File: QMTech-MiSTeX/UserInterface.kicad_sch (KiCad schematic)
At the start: 58 parts, among them CN2 U.FL-R-SMT-1(80), CN3 U.FL-R-SMT-1(80), CN4 U.FL-R-SMT-1(80), CN5 U.FL-R-SMT-1(80), CN6 U.FL-R-SMT-1(80), CN7 U.FL-R-SMT-1(80), SW1 TS-1187A-B-A-B, SW2 TS-1187A-B-A-B, SW3 TS-1187A-B-A-B, SW4 TS-1187A-B-A-B, SW5 XKB5858-W-F-75

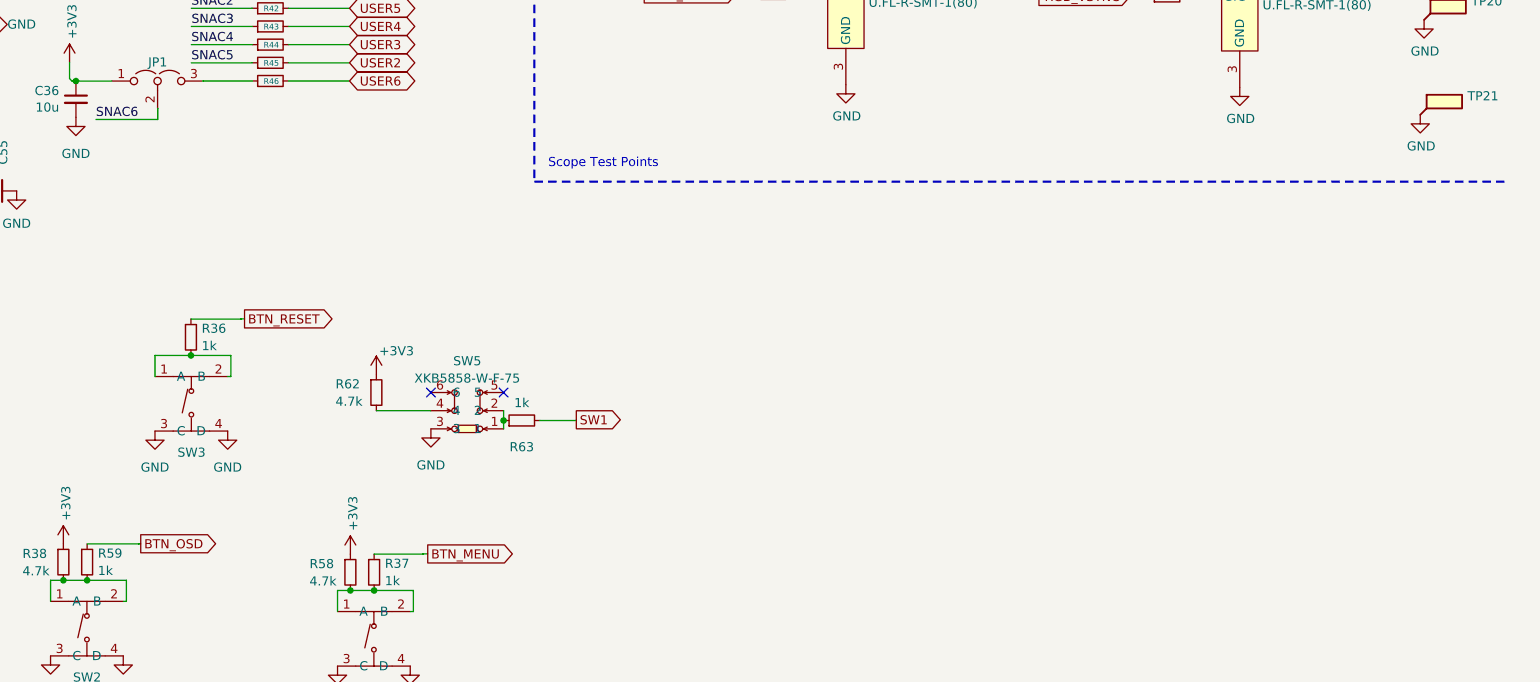
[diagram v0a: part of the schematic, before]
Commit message: connect two remaining pins to new 2 row Pmod, fix via, tidy test points
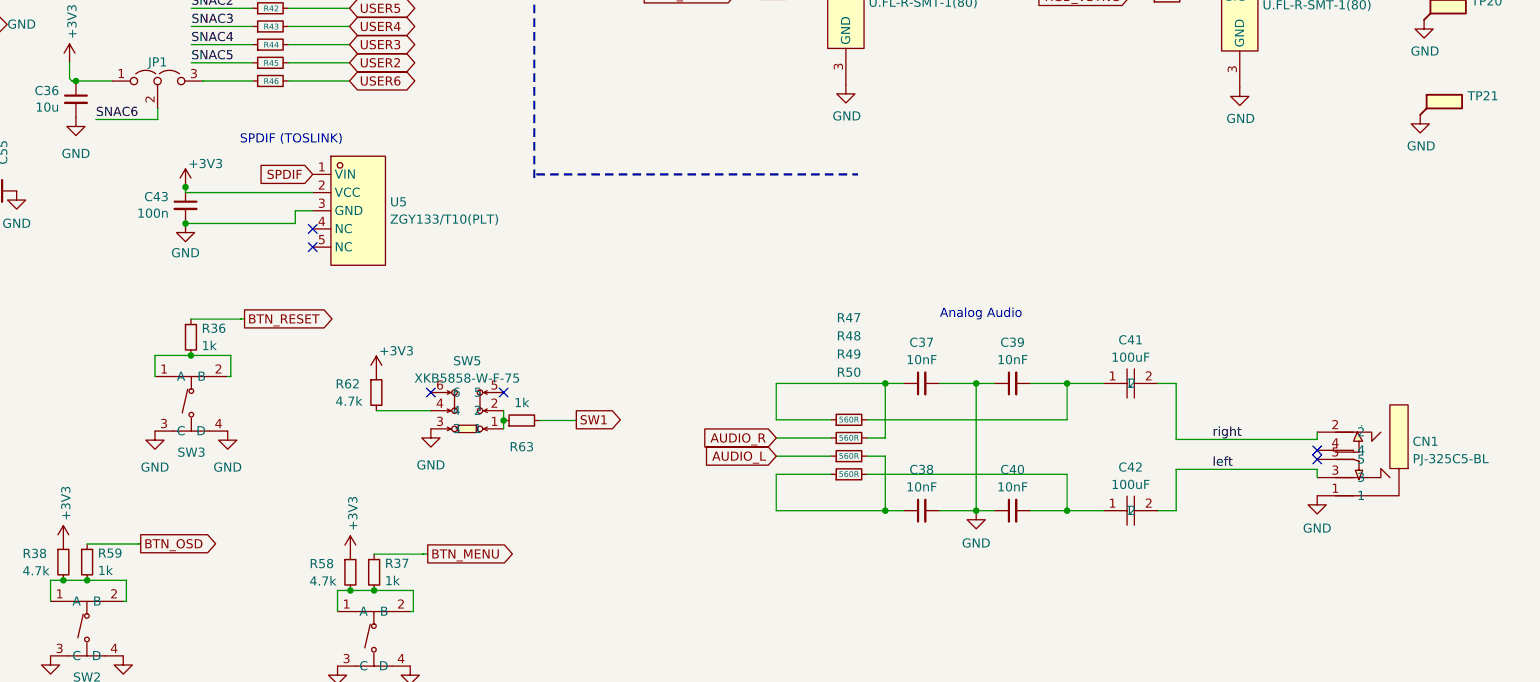
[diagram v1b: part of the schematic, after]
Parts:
- added C37, C38, C39, C40: 10nF, C_0402_1005Metric, symbol jlcpcb-basic-mlcc-0402:10nF
- added C41, C42: 100uF, easyeda2kicad:C1206, symbol easyeda2kicad:CL31A107MQHNNNE
- added C43: 100n, Capacitor_SMD:C_0603_1608Metric, symbol Device:C_Small
- added CN1: PJ-325C5-BL, easyeda2kicad:TH_PJ-325C5-B, symbol easyeda2kicad:PJ-325C5-BL
- added R47, R48, R49, R50: 560R, R_0603_1608Metric, symbol jlcpcb-basic-resistor-0603:560R
- added U5: ZGY133/T10(PLT), easyeda2kicad:COMM-TH_ZGY133-T10-PLT, symbol easyeda2kicad:ZGY133_T10(PLT)
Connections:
- net +3V3: now also C43.1, U5.2 (VCC)
- net GND: now also C37.2, C38.2, C39.1, C40.1, C43.2, CN1.1, U5.3 (GND)
- net SPDIF: now also U5.1 (VIN)
- new net: C37.1, R47.1, R48.2
- new net: C39.2, C41.1, R47.2
- new net: C38.1, R49.2, R50.1
- new net: C40.2, C42.1, R50.2
- new net AUDIO_L: R49.1
- new net AUDIO_R: R48.1
- new net left: C42.2, CN1.3
- new net right: C41.2, CN1.2
- no-connect marks 4 -> 8
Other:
- note added: "Analog Audio"
- note added: "SPDIF (TOSLINK)"
- note removed: "Scope Test Points"

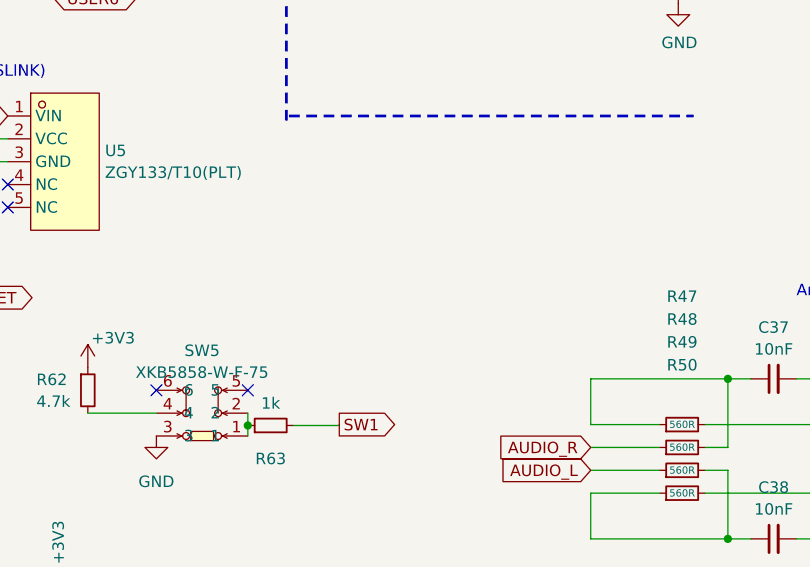
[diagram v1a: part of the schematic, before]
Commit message: add front switch, reroute USB, test points
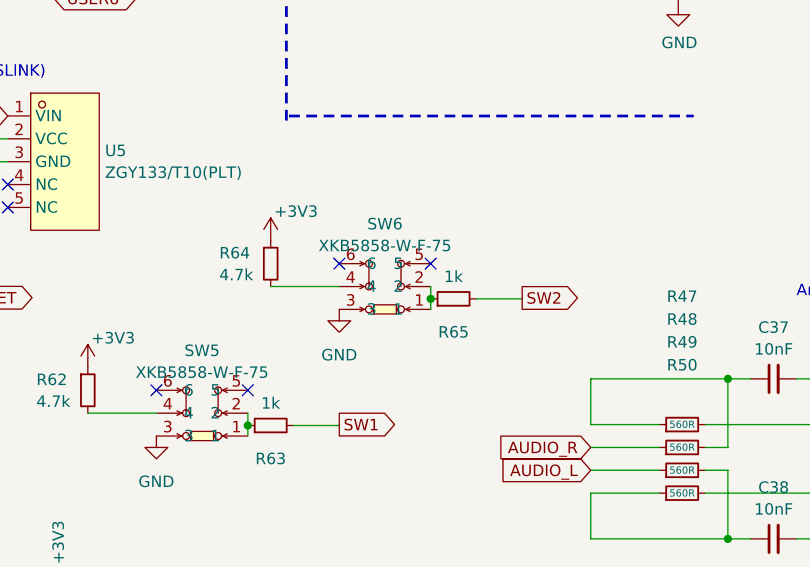
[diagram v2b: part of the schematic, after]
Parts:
- added R64: 4.7k, R_0402_1005Metric, symbol jlcpcb-basic-resistor:R_0402_4.7k
- added R65: 1k, R_0402_1005Metric, symbol jlcpcb-basic-resistor-0402:1k
- added SW6: XKB5858-W-F-75, easyeda2kicad:SW-SMD_XKB5858-W-F-75, symbol easyeda2kicad:XKB5858-W-F-75
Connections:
- net +3V3: now also R64.1
- net GND: now also SW6.3
- new net: R65.1, SW6.1, SW6.2
- new net: R64.2, SW6.4
- new net SW2: R65.2
- no-connect marks 8 -> 10
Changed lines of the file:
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@@
   (junction (at 92.71 121.158) (diameter 0) (color 0 0 0 0)
   )
+  (junction (at 157.48 134.62) (diameter 0) (color 0 0 0 0)
+  )
   (junction (at 55.7022 66.7512) (diameter 0) (color 0 0 0 0)
   )
@@
   (no_connect (at 250.8504 152.8572))
   (no_connect (at 110.49 124.46))
+  (no_connect (at 147.32 130.7099))
+  (no_connect (at 157.48 130.7099))
   (no_connect (at 35.0774 88.2396))
   (no_connect (at 127 144.78))
@@
     (stroke (width 0) (type default))
   )
+  (wire (pts (xy 162.56 134.62) (xy 167.64 134.62))
+    (stroke (width 0) (type default))
+  )
   (wire (pts (xy 137.16 147.32) (xy 137.16 148.6901))
     (stroke (width 0) (type default))
@@
     (stroke (width 0) (type default))
   )
+  (wire (pts (xy 157.48 133.2499) (xy 157.48 134.62))
+    (stroke (width 0) (type default))
+  )
   (wire (pts (xy 198.12 143.51) (xy 203.2 143.51))
     (stroke (width 0) (type default))
@@
     (stroke (width 0) (type default))
   )
+  (wire (pts (xy 157.48 134.62) (xy 157.48 135.7899))
+    (stroke (width 0) (type default))
+  )
   (wire (pts (xy 93.5171 96.1644) (xy 102.0318 96.1644))
     (stroke (width 0) (type default))
@@
     (stroke (width 0) (type default))
   )
+  (wire (pts (xy 139.7 133.2499) (xy 147.32 133.2499))
+    (stroke (width 0) (type default))
+  )
   (wire (pts (xy 84.9687 52.7558) (xy 76.454 52.7558))
     (stroke (width 0) (type default))
@@
     (stroke (width 0.254) (type default))
   )
+  (wire (pts (xy 167.64 134.62) (xy 167.64 134.5199))
+    (stroke (width 0) (type default))
+  )
   (wire (pts (xy 228.6 143.51) (xy 231.14 143.51))
     (stroke (width 0.254) (type default))
@@
     )
   )
+  (global_label "SW2" (shape output) (at 167.64 134.5199 0) (fields_autoplaced)
+    (effects (font (size 1.27 1.27)) (justify left))
+    (property "Intersheetrefs" "${INTERSHEET_REFS}" (at 174.5907 134.5199 0)
+      (effects (font (size 1.27 1.27)) (justify left))
+    )
+  )
   (global_label "BTN_MENU" (shape output) (at 126.5557 167.3352 0) (fields_autoplaced)
     (effects (font (size 1.27 1.27)) (justify left))
@@
     )
   )
+  (symbol (lib_id "power:+3V3") (at 139.7 128.1699 0) (unit 1)
+    (in_bom yes) (on_board yes) (dnp no)
+    (property "Reference" "#PWR0186" (at 139.7 131.9799 0)
+      (effects (font (size 1.27 1.27)) hide)
+    )
+    (property "Value" "+3V3" (at 140.081 124.9187 0)
+      (effects (font (size 1.27 1.27)) (justify left))
+    )
+    (property "Footprint" "" (at 139.7 128.1699 0)
+      (effects (font (size 1.27 1.27)) hide)
+    )
+    (property "Datasheet" "" (at 139.7 128.1699 0)
+      (effects (font (size 1.27 1.27)) hide)
+    )
+    (pin "1")
+    (instances
+      (project "QMTech-MiSTeX"
+        (path "/bf95850e-2fcb-4784-a603-f17fc357556b/cce2b405-ae09-44af-ba42-d113d6ffe521"
+          (reference "#PWR0186") (unit 1)
+        )
+      )
+    )
+  )
   (symbol (lib_id "jlcpcb-basic-resistor-0402:1k") (at 227.5078 36.5506 90) (unit 1)
     (in_bom yes) (on_board yes) (dnp no) (fields_autoplaced)
@@
     )
   )
+  (symbol (lib_id "easyeda2kicad:XKB5858-W-F-75") (at 152.4 133.2499 90) (unit 1)
+    (in_bom yes) (on_board yes) (dnp no) (fields_autoplaced)
+    (property "Reference" "SW6" (at 152.4 126.3126 90)
+      (effects (font (size 1.27 1.27)))
+    )
+    (property "Value" "XKB5858-W-F-75" (at 152.4 128.7368 90)
+      (effects (font (size 1.27 1.27)))
+    )
+    (property "Footprint" "easyeda2kicad:SW-SMD_XKB5858-W-F-75" (at 165.1 133.2499 0)
+      (effects (font (size 1.27 1.27)) hide)
+    )
+    (property "Datasheet" "https://lcsc.com/product-detail/Electrical-Switches_XKB-Connectivity-XKB5858-W-F-75_C780037.html" (at 167.64 133.2499 0)
+      (effects (font (size 1.27 1.27)) hide)
+    )
+    (property "LCSC Part" "C780037" (at 170.18 133.2499 0)
+      (effects (font (size 1.27 1.27)) hide)
+    )
+    (pin "2")
+    (pin "1")
+    (pin "4")
+    (pin "5")
+    (pin "3")
+    (pin "6")
+    (instances
+      (project "QMTech-MiSTeX"
+        (path "/bf95850e-2fcb-4784-a603-f17fc357556b/cce2b405-ae09-44af-ba42-d113d6ffe521"
+          (reference "SW6") (unit 1)
+        )
+      )
+    )
+  )
   (symbol (lib_id "easyeda2kicad:TS-1187A-B-A-B") (at 119.0324 177.927 0) (unit 1)
     (in_bom yes) (on_board yes) (dnp no)
@@
     )
   )
+  (symbol (lib_id "jlcpcb-basic-resistor:R_0402_4.7k") (at 139.7 130.7099 0) (unit 1)
+    (in_bom yes) (on_board yes) (dnp no)
+    (property "Reference" "R64" (at 133.985 129.5415 0)
+      (effects (font (size 1.27 1.27)) (justify left))
+    )
+    (property "Value" "4.7k" (at 133.985 131.9657 0)
+      (effects (font (size 1.27 1.27)) (justify left))
+    )
+    (property "Footprint" "R_0402_1005Metric" (at 137.922 130.7099 90)
+      (effects (font (size 1.27 1.27)) hide)
+    )
+    (property "Datasheet" "https://datasheet.lcsc.com/szlcsc/Uniroyal-Elec-0402WGF4701TCE_C25900.pdf" (at 139.7 130.7099 90)
+      (effects (font (size 1.27 1.27)) hide)
+    )
+    (property "LCSC" "C25900" (at 139.7 130.7099 90)
+      (effects (font (size 1.27 1.27)) hide)
+    )
+    (pin "2")
+    (pin "1")
+    (instances
+      (project "QMTech-MiSTeX"
+        (path "/bf95850e-2fcb-4784-a603-f17fc357556b/cce2b405-ae09-44af-ba42-d113d6ffe521"
+          (reference "R64") (unit 1)
+        )
+      )
+    )
+  )
   (symbol (lib_id "jlcpcb-basic-resistor-0603:560R") (at 52.959 126.6698 180) (unit 1)
     (in_bom yes) (on_board yes) (dnp no) (fields_autoplaced)
@@
     )
   )
+  (symbol (lib_id "jlcpcb-basic-resistor-0402:1k") (at 160.02 134.62 90) (unit 1)
+    (in_bom yes) (on_board yes) (dnp no)
+    (property "Reference" "R65" (at 160.02 138.3299 90)
+      (effects (font (size 1.27 1.27)))
+    )
+    (property "Value" "1k" (at 160.02 132.1633 90)
+      (effects (font (size 1.27 1.27)))
+    )
+    (property "Footprint" "R_0402_1005Metric" (at 160.02 136.398 90)
+      (effects (font (size 1.27 1.27)) hide)
+    )
+    (property "Datasheet" "https://datasheet.lcsc.com/szlcsc/Uniroyal-Elec-0402WGF1001TCE_C11702.pdf" (at 160.02 134.62 90)
+      (effects (font (size 1.27 1.27)) hide)
+    )
+    (property "LCSC" "C11702" (at 160.02 134.62 90)
+      (effects (font (size 1.27 1.27)) hide)
+    )
+    (pin "2")
+    (pin "1")
+    (instances
+      (project "QMTech-MiSTeX"
+        (path "/bf95850e-2fcb-4784-a603-f17fc357556b/cce2b405-ae09-44af-ba42-d113d6ffe521"
+          (reference "R65") (unit 1)
+        )
+      )
+    )
+  )
   (symbol (lib_id "Device:C_Small") (at 92.71 118.618 0) (mirror y) (unit 1)
     (in_bom yes) (on_board yes) (dnp no)
@@
         )
       )
+    )
+  )
+  (symbol (lib_id "power:GND") (at 147.32 135.7899 0) (unit 1)
+    (in_bom yes) (on_board yes) (dnp no) (fields_autoplaced)
+    (property "Reference" "#PWR0187" (at 147.32 142.1399 0)
+      (effects (font (size 1.27 1.27)) hide)
+    )
+    (property "Value" "GND" (at 147.32 140.8699 0)
+      (effects (font (size 1.27 1.27)))
+    )
+    (property "Footprint" "" (at 147.32 135.7899 0)
+      (effects (font (size 1.27 1.27)) hide)
+    )
+    (property "Datasheet" "" (at 147.32 135.7899 0)
+      (effects (font (size 1.27 1.27)) hide)
+    )
+    (pin "1")
+    (instances
+      (project "QMTech-MiSTeX"
+        (path "/bf95850e-2fcb-4784-a603-f17fc357556b/cce2b405-ae09-44af-ba42-d113d6ffe521"
+          (reference "#PWR0187") (unit 1)
+        )
+      )

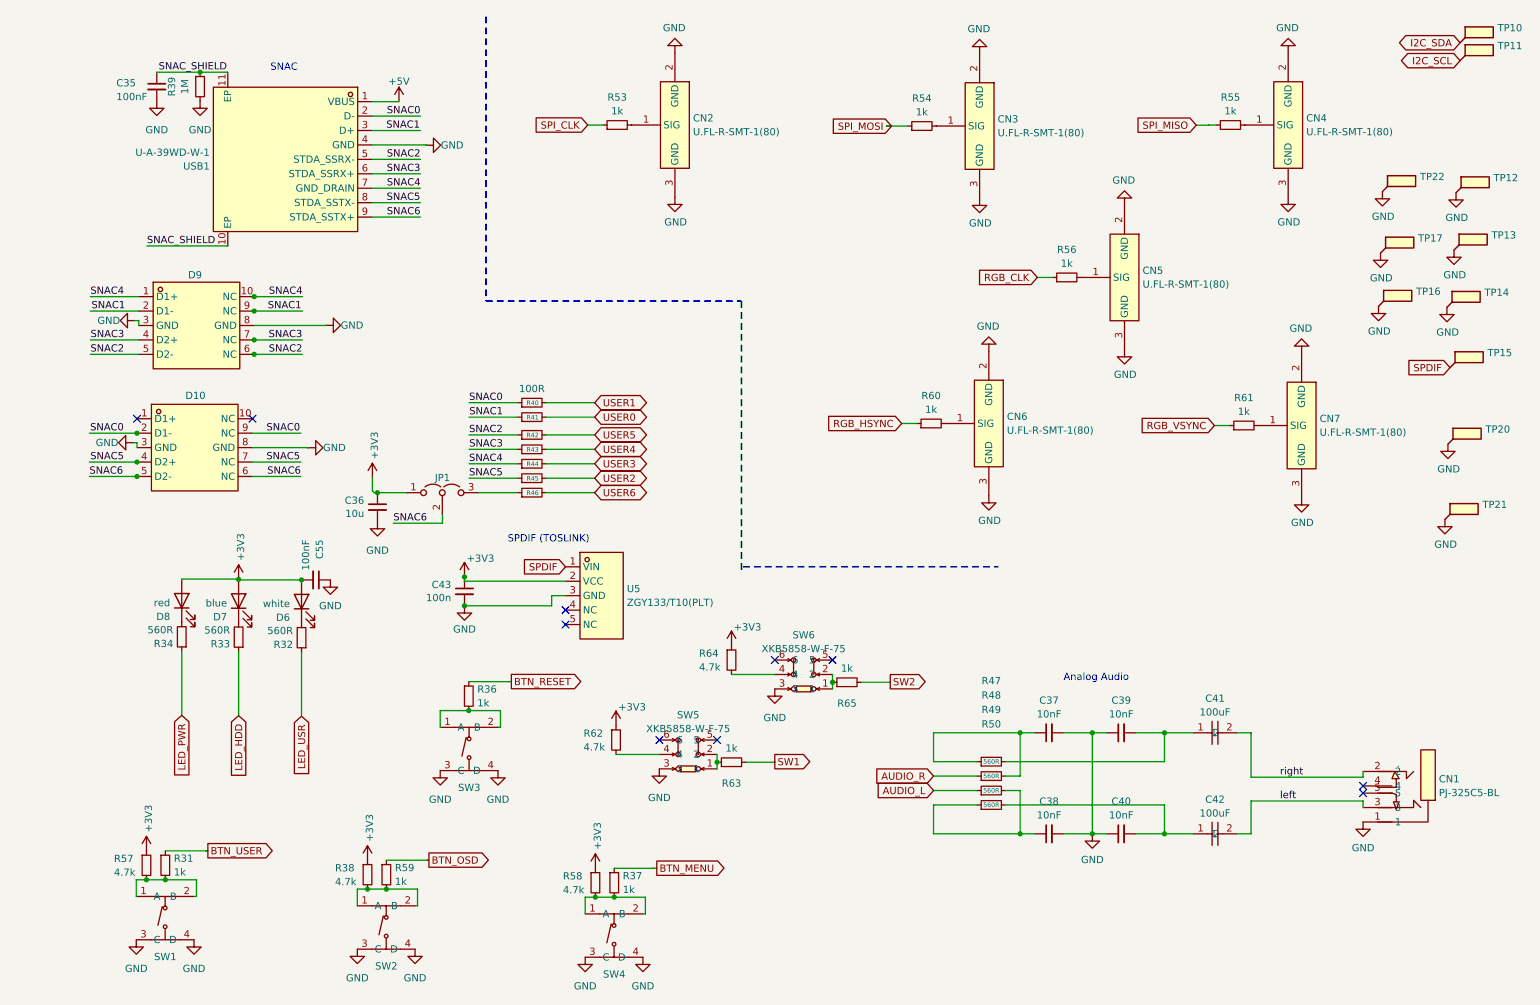
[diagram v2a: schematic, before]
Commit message: Add VGA green probe, add DIP switches, add to silk screen, cosmetics
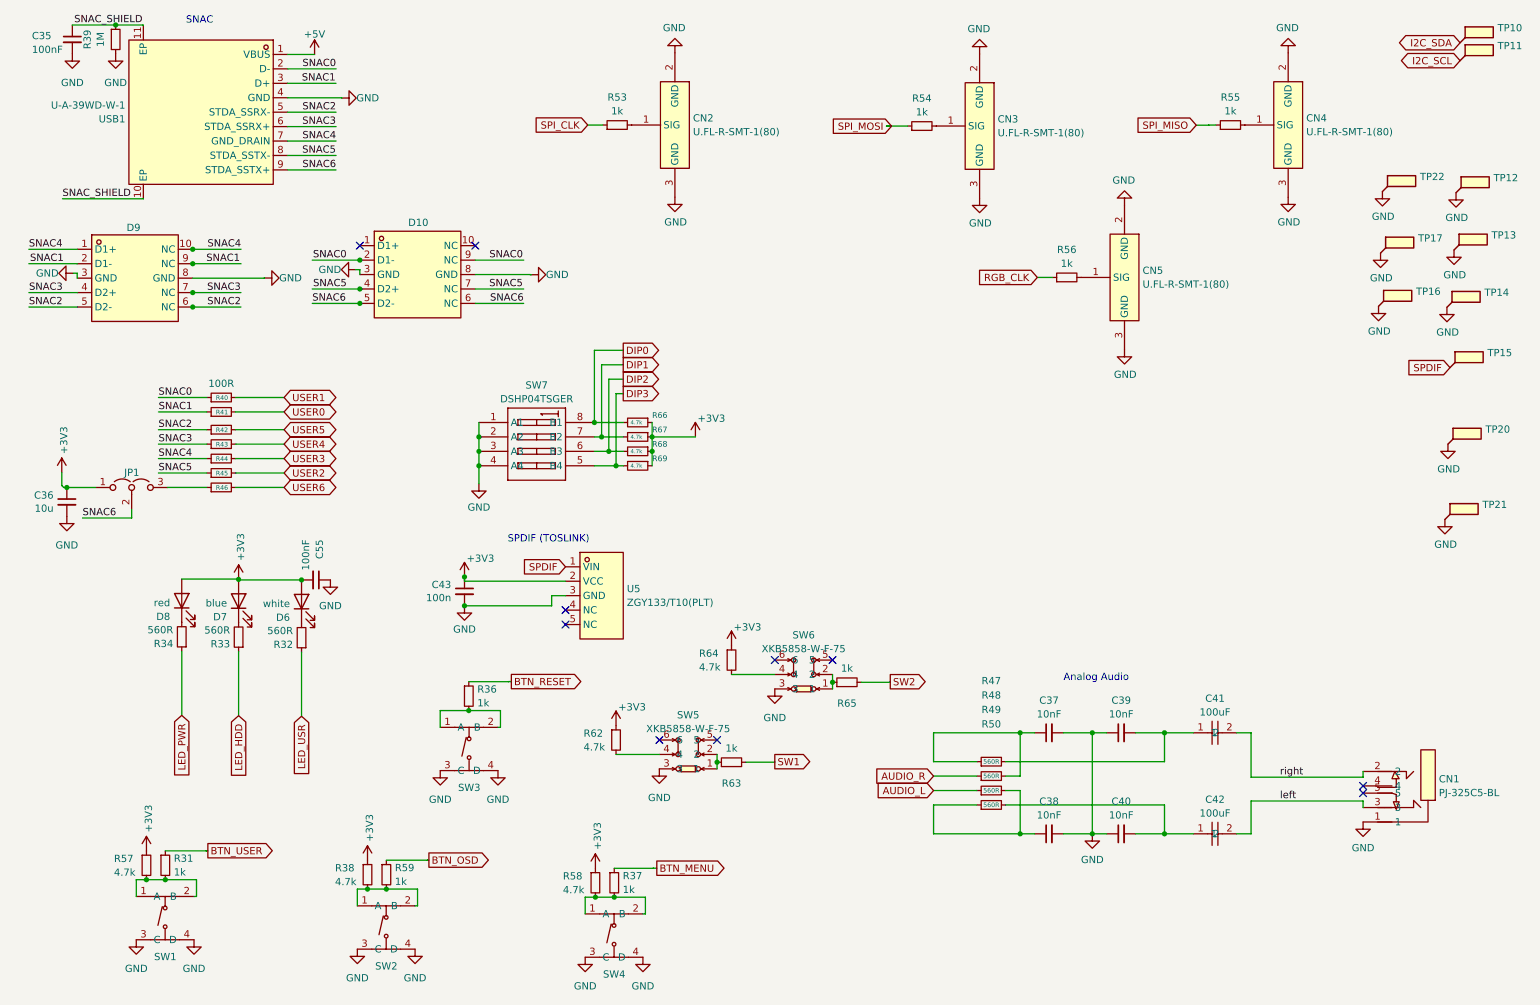
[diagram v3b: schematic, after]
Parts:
- removed CN6, CN7: U.FL-R-SMT-1(80), easyeda2kicad:RF-SMD_FRF05002-JSS103M, symbol easyeda2kicad:U.FL-R-SMT-1(80)
- removed R60, R61: 1k, R_0402_1005Metric, symbol jlcpcb-basic-resistor-0402:1k
- added R66, R67, R68, R69: 4.7k, R_0402_1005Metric, symbol jlcpcb-basic-resistor:R_0402_4.7k
- added SW7: DSHP04TSGER, easyeda2kicad:SW-SMD_8P-L6.7-W5.4-P1.27-LS8.4, symbol easyeda2kicad:DSHP04TSGER
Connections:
- net +3V3: now also R66.1, R67.1, R68.1, R69.1
- net GND: now also SW7.1 (A1), SW7.2 (A2), SW7.3 (A3), SW7.4 (A4)
- new net DIP0: R66.2, SW7.8 (B1)
- new net DIP1: R67.2, SW7.7 (B2)
- new net DIP2: R68.2, SW7.6 (B3)
- new net DIP3: R69.2, SW7.5 (B4)
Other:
- moved on the sheet: C35, C36, D10, D9, JP1, R39, R40, R41, R42, R43, R44, R45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
